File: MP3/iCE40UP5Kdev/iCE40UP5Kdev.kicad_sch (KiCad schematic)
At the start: 51 parts, among them J1 USB4105-GF-A, J2 Left, J3 Right, U1 W25Q32JV, U2 MIC5365-1-2YD5, U3 MIC5318-3-3YD5, U4 ICE40UP5K-SG48ITR, X1 IQXO-791

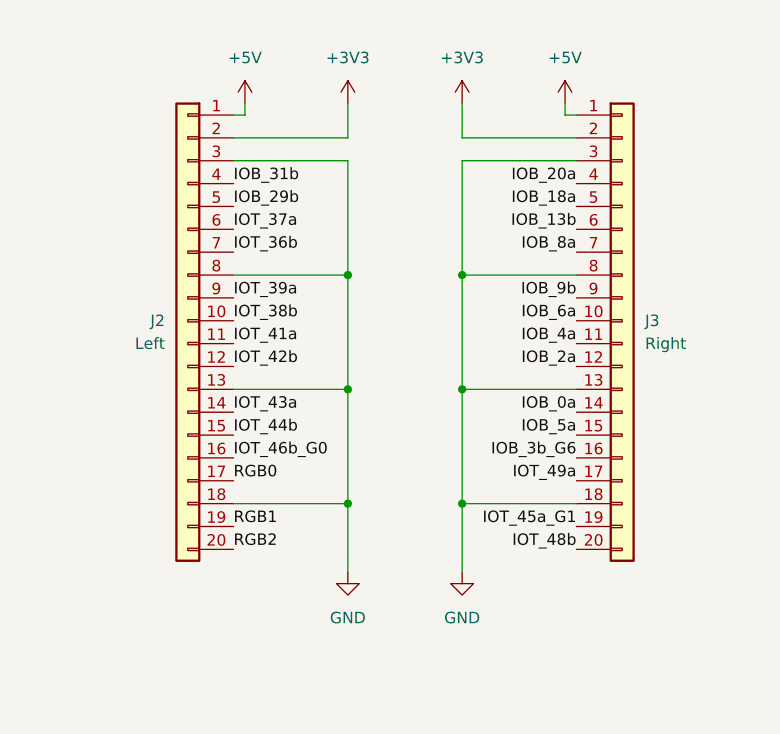
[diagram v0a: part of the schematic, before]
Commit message: Implementing Feedback
- Made USB D+, D- on one plane and made the path shorter
- Used correct footprint for FPGA Chip
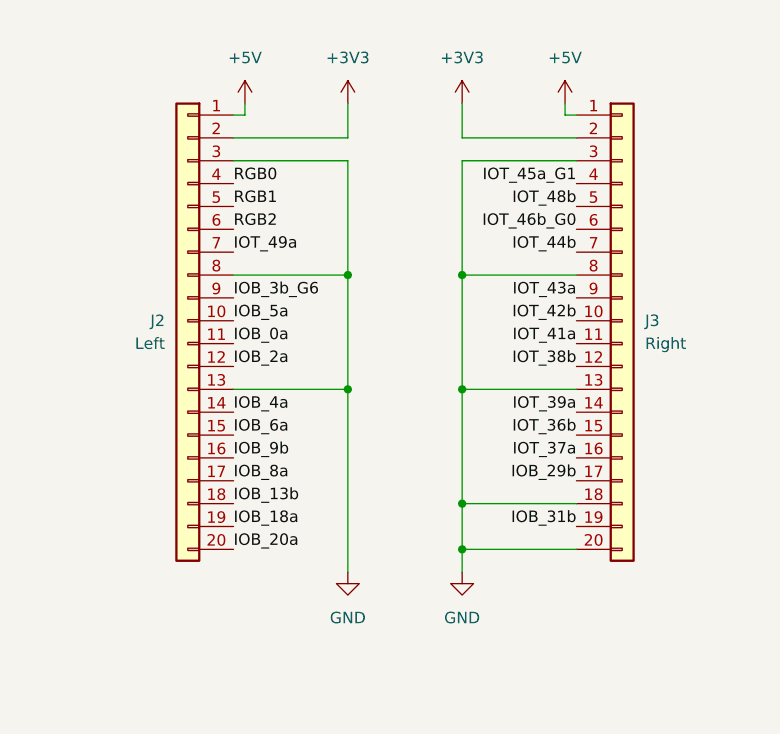
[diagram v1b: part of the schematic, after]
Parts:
- U4: footprint Eclectronics:QFN48_L-ASC10_ICE40ULTRAPLUS_MACHXO2_LAT -> Package_DFN_QFN:QFN-48-1EP_7x7mm_P0.5mm_EP5.6x5.6mm
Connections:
- net GND: now also J3.20 (Pin_20); no longer J2.18 (Pin_18)
- net IOB_0a: now also J2.11 (Pin_11); no longer J3.14 (Pin_14)
- net IOB_13b: now also J2.18 (Pin_18); no longer J3.6 (Pin_6)
- net IOB_18a: now also J2.19 (Pin_19); no longer J3.5 (Pin_5)
- net IOB_20a: now also J2.20 (Pin_20); no longer J3.4 (Pin_4)
- net IOB_29b: now also J3.17 (Pin_17); no longer J2.5 (Pin_5)
- net IOB_2a: now also J2.12 (Pin_12); no longer J3.12 (Pin_12)
- net IOB_31b: now also J3.19 (Pin_19); no longer J2.4 (Pin_4)
- net IOB_3b_G6: now also J2.9 (Pin_9); no longer J3.16 (Pin_16)
- net IOB_4a: now also J2.14 (Pin_14); no longer J3.11 (Pin_11)
- net IOB_5a: now also J2.10 (Pin_10); no longer J3.15 (Pin_15)
- net IOB_6a: now also J2.15 (Pin_15); no longer J3.10 (Pin_10)
- net IOB_8a: now also J2.17 (Pin_17); no longer J3.7 (Pin_7)
- net IOB_9b: now also J2.16 (Pin_16); no longer J3.9 (Pin_9)
- net IOT_36b: now also J3.15 (Pin_15); no longer J2.7 (Pin_7)
- net IOT_37a: now also J3.16 (Pin_16); no longer J2.6 (Pin_6)
- net IOT_38b: now also J3.12 (Pin_12); no longer J2.10 (Pin_10)
- net IOT_39a: now also J3.14 (Pin_14); no longer J2.9 (Pin_9)
- net IOT_41a: now also J3.11 (Pin_11); no longer J2.11 (Pin_11)
- net IOT_42b: now also J3.10 (Pin_10); no longer J2.12 (Pin_12)
- net IOT_43a: now also J3.9 (Pin_9); no longer J2.14 (Pin_14)
- net IOT_44b: now also J3.7 (Pin_7); no longer J2.15 (Pin_15)
- net IOT_45a_G1: now also J3.4 (Pin_4); no longer J3.19 (Pin_19)
- net IOT_46b_G0: now also J3.6 (Pin_6); no longer J2.16 (Pin_16)
- net IOT_48b: now also J3.5 (Pin_5); no longer J3.20 (Pin_20)
- net IOT_49a: now also J2.7 (Pin_7); no longer J3.17 (Pin_17)
- net RGB0: now also J2.4 (Pin_4); no longer J2.17 (Pin_17)
- net RGB1: now also J2.5 (Pin_5); no longer J2.19 (Pin_19)
- net RGB2: now also J2.6 (Pin_6); no longer J2.20 (Pin_20)
